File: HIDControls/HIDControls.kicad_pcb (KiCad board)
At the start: 2 copper layers, 83.8 x 91.4 mm, 65 parts, among them J1 AnalogJoystick, M1 ModulePlug, M10 ModulePlug, M11 ModulePlug, M12 ModulePlug, M2 ModulePlug, M3 ModulePlug, M4 ModulePlug, M5 ModulePlug, M6 ModulePlug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

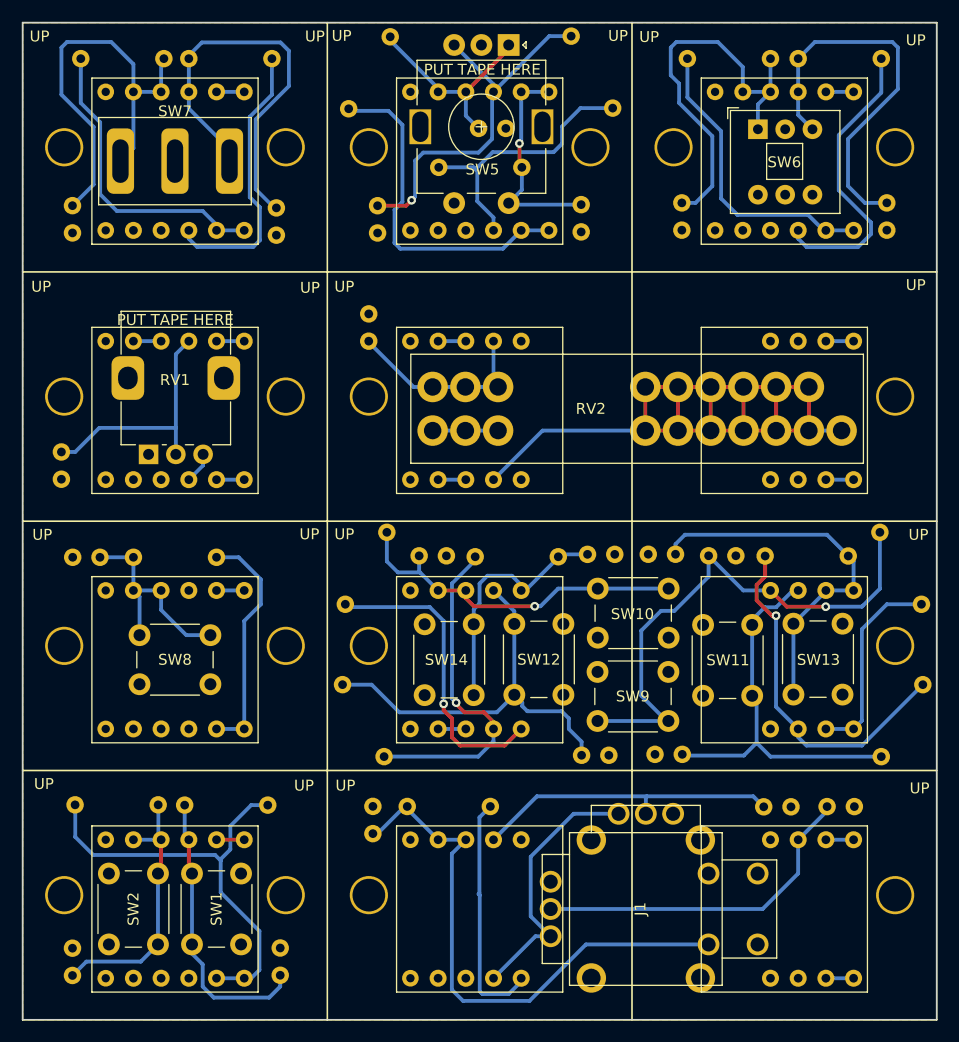
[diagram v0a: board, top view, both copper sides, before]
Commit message: Separate fills for each control
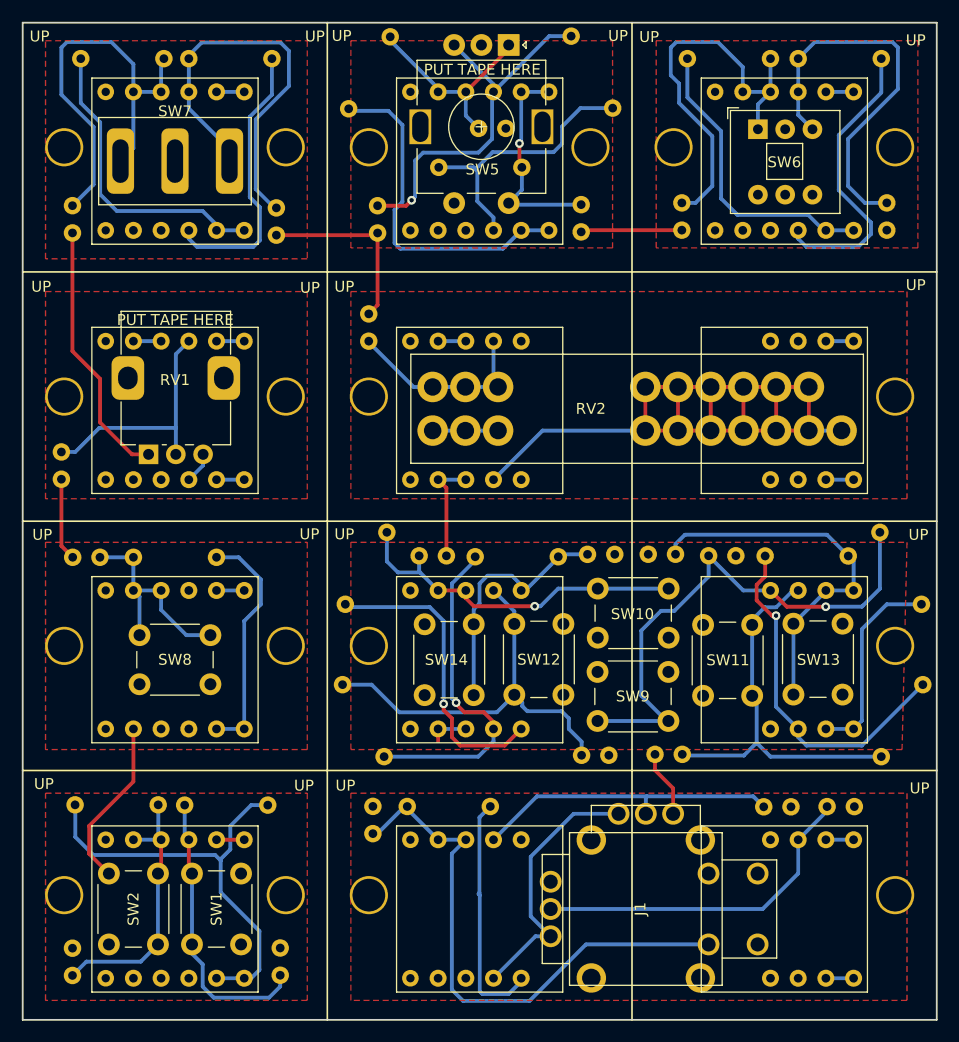
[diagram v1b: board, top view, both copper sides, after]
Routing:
- net GND: track 11.1 -> 99.4 mm
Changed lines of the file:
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@@
   (segment (start 101.6 82.55) (end 99.06 82.55) (width 0.35) (layer "B.Cu") (net 2))
   (segment (start 129.54 82.55) (end 127 82.55) (width 0.35) (layer "B.Cu") (net 5))
+  (segment (start 127 119.23) (end 127 118.11) (width 0.35) (layer "F.Cu") (net 6))
+  (segment (start 112.17 72.83) (end 121.25 72.83) (width 0.35) (layer "F.Cu") (net 6))
+  (segment (start 99.06 122.94) (end 95 127) (width 0.35) (layer "F.Cu") (net 6))
+  (segment (start 100.45 92.93) (end 98.93 92.93) (width 0.35) (layer "F.Cu") (net 6))
+  (segment (start 121.45 79.24) (end 120.64 80.05) (width 0.35) (layer "F.Cu") (net 6))
+  (segment (start 146.89 121.89) (end 148.55 123.55) (width 0.35) (layer "F.Cu") (net 6))
+  (segment (start 93.472 83.472) (end 93.472 72.624) (width 0.35) (layer "F.Cu") (net 6))
+  (segment (start 146.89 120.44) (end 146.89 121.89) (width 0.35) (layer "F.Cu") (net 6))
+  (segment (start 148.55 123.55) (end 148.55 125.89) (width 0.35) (layer "F.Cu") (net 6))
+  (segment (start 140.28 72.37) (end 140.12 72.53) (width 0.35) (layer "F.Cu") (net 6))
+  (segment (start 127.762 102.235) (end 127.762 96.012) (width 0.35) (layer "F.Cu") (net 6))
+  (segment (start 99.06 118.11) (end 99.06 122.94) (width 0.35) (layer "F.Cu") (net 6))
+  (segment (start 98.93 92.93) (end 96 90) (width 0.35) (layer "F.Cu") (net 6))
+  (segment (start 96 86) (end 93.472 83.472) (width 0.35) (layer "F.Cu") (net 6))
+  (segment (start 121.25 72.83) (end 121.45 72.63) (width 0.35) (layer "F.Cu") (net 6))
+  (segment (start 121.45 72.63) (end 121.45 79.24) (width 0.35) (layer "F.Cu") (net 6))
+  (segment (start 92.456 95.21) (end 92.456 101.332) (width 0.35) (layer "F.Cu") (net 6))
+  (segment (start 149.352 72.37) (end 140.28 72.37) (width 0.35) (layer "F.Cu") (net 6))
+  (segment (start 92.456 101.332) (end 93.492 102.368) (width 0.35) (layer "F.Cu") (net 6))
+  (segment (start 95 129.56) (end 96.81 131.37) (width 0.35) (layer "F.Cu") (net 6))
+  (segment (start 96 90) (end 96 86) (width 0.35) (layer "F.Cu") (net 6))
+  (segment (start 127.762 96.012) (end 127 95.25) (width 0.35) (layer "F.Cu") (net 6))
+  (segment (start 95 127) (end 95 129.56) (width 0.35) (layer "F.Cu") (net 6))
   (segment (start 129.54 95.25) (end 127 95.25) (width 0.35) (layer "B.Cu") (net 6))
   (segment (start 129.54 118.11) (end 127 118.11) (width 0.35) (layer "B.Cu") (net 6))
@@
     (polygon
       (pts
-        (xy 172.72 144.78)
-        (xy 88.9 144.78)
-        (xy 88.9 53.34)
-        (xy 172.72 53.34)
-      )
-    )
+        (xy 143 74)
+        (xy 119 74)
+        (xy 119 55)
+        (xy 143 55)
+      )
+    )
+  )
+  (zone (net 6) (net_name "GND") (layer "F.Cu") (hatch edge 0.508)
+    (connect_pads (clearance 0.508))
+    (min_thickness 0.254) (filled_areas_thickness no)
+    (fill yes (thermal_gap 0.508) (thermal_bridge_width 0.508))
+    (polygon
+      (pts
+        (xy 115 75)
+        (xy 91 75)
+        (xy 91 55)
+        (xy 115 55)
+      )
+    )
+  )
+  (zone (net 6) (net_name "GND") (layer "F.Cu") (hatch edge 0.508)
+    (connect_pads (clearance 0.508))
+    (min_thickness 0.254) (filled_areas_thickness no)
+    (fill yes (thermal_gap 0.508) (thermal_bridge_width 0.508))
+    (polygon
+      (pts
+        (xy 169.545 120)
+        (xy 119 120)
+        (xy 119 101)
+        (xy 170 101)
+      )
+    )
+  )
+  (zone (net 6) (net_name "GND") (layer "F.Cu") (hatch edge 0.508)
+    (connect_pads (clearance 0.508))
+    (min_thickness 0.254) (filled_areas_thickness no)
+    (fill yes (thermal_gap 0.508) (thermal_bridge_width 0.508))
+    (polygon
+      (pts
+        (xy 171 74)
+        (xy 147 74)
+        (xy 147 55)
+        (xy 171 55)
+      )
+    )
+  )
+  (zone (net 6) (net_name "GND") (layer "F.Cu") (hatch edge 0.508)
+    (connect_pads (clearance 0.508))
+    (min_thickness 0.254) (filled_areas_thickness no)
+    (fill yes (thermal_gap 0.508) (thermal_bridge_width 0.508))
+    (polygon
+      (pts
+        (xy 115 143)
+        (xy 91 143)
+        (xy 91 124)
+        (xy 115 124)
+      )
+    )
+  )
+  (zone (net 6) (net_name "GND") (layer "F.Cu") (hatch edge 0.508)
+    (connect_pads (clearance 0.508))
+    (min_thickness 0.254) (filled_areas_thickness no)
+    (fill yes (thermal_gap 0.508) (thermal_bridge_width 0.508))
+    (polygon
+      (pts
+        (xy 170 97)
+        (xy 119 97)
+        (xy 119 78)
+        (xy 170 78)
+      )
+    )
+  )
+  (zone (net 6) (net_name "GND") (layer "F.Cu") (hatch edge 0.508)
+    (connect_pads (clearance 0.508))
+    (min_thickness 0.254) (filled_areas_thickness no)
+    (fill yes (thermal_gap 0.508) (thermal_bridge_width 0.508))
+    (polygon
+      (pts
+        (xy 170 143)
+        (xy 119 143)
+        (xy 119 124)
+        (xy 170 124)
+      )
+    )
+  )
+  (zone (net 6) (net_name "GND") (layer "F.Cu") (hatch edge 0.508)
+    (connect_pads (clearance 0.508))
+    (min_thickness 0.254) (filled_areas_thickness no)
+    (fill yes (thermal_gap 0.508) (thermal_bridge_width 0.508))
+    (polygon
+      (pts
+        (xy 115 97)
+        (xy 91 97)
+        (xy 91 78)
+        (xy 115 78)
+      )
+    )
+  )
+  (zone (net 6) (net_name "GND") (layer "F.Cu") (hatch edge 0.508)
+    (connect_pads (clearance 0.508))
+    (min_thickness 0.254) (filled_areas_thickness no)
+    (fill yes (thermal_gap 0.508) (thermal_bridge_width 0.508))
+    (polygon
+      (pts
+        (xy 115 120)
+        (xy 91 120)
+        (xy 91 101)
+        (xy 115 101)
+      )
+    )

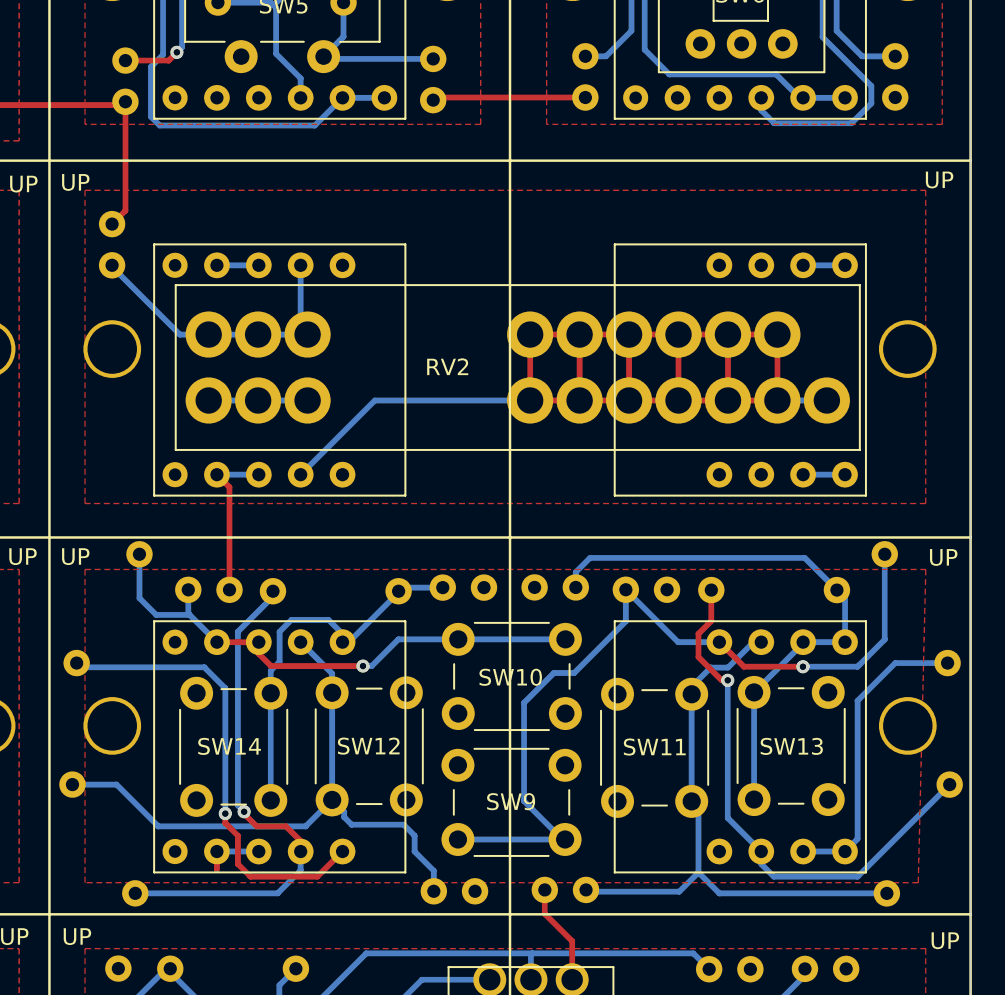
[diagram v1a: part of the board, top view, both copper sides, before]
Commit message: A few layout tweaks
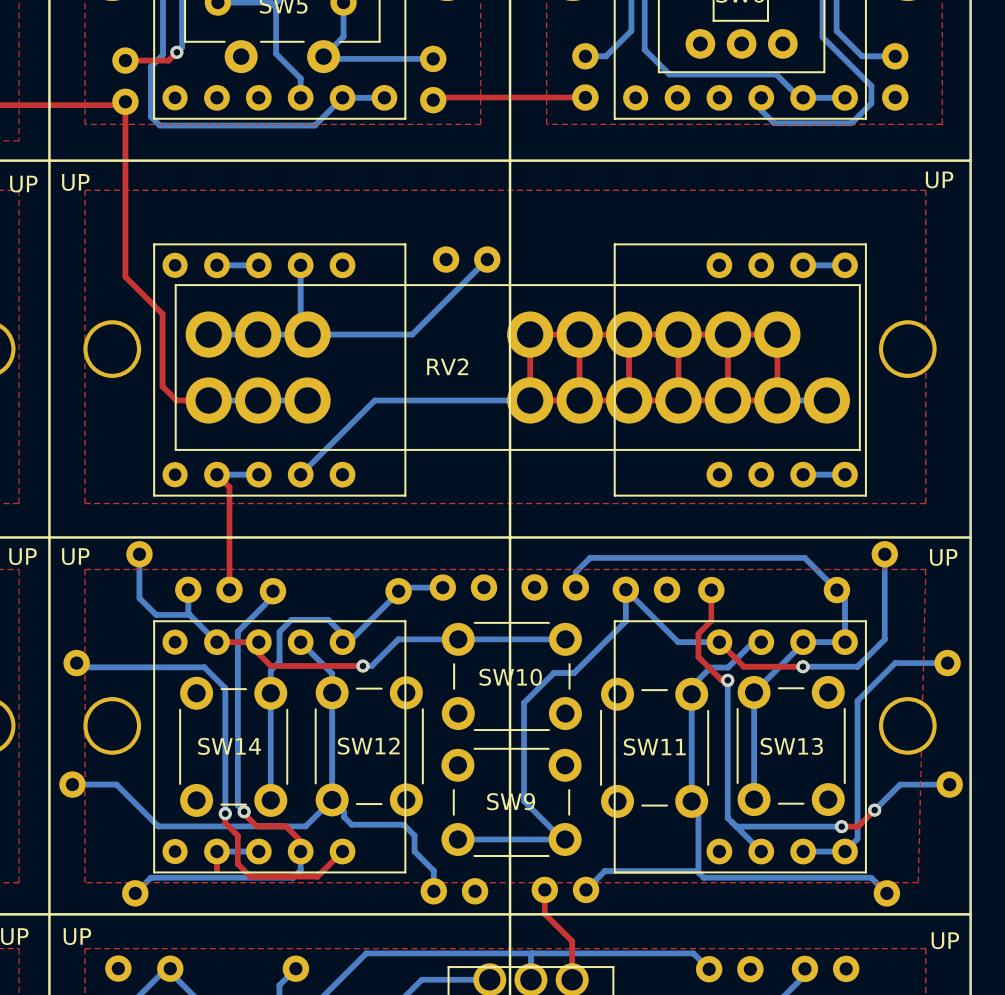
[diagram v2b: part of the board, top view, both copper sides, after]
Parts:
- moved C2 20.4 mm to (140.9, 82.2), turned to 0 degrees
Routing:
- net GND: track 99.4 -> 113.0 mm
- net Net-(C2-Pad2): track 18.0 -> 23.2 mm
- net Net-(M10-Pad2): track 32.8 -> 32.3 mm, vias 1 -> 3
